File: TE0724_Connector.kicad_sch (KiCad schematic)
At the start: 1 part, among them J1 SS5-80-3.50-X-D-K-XX

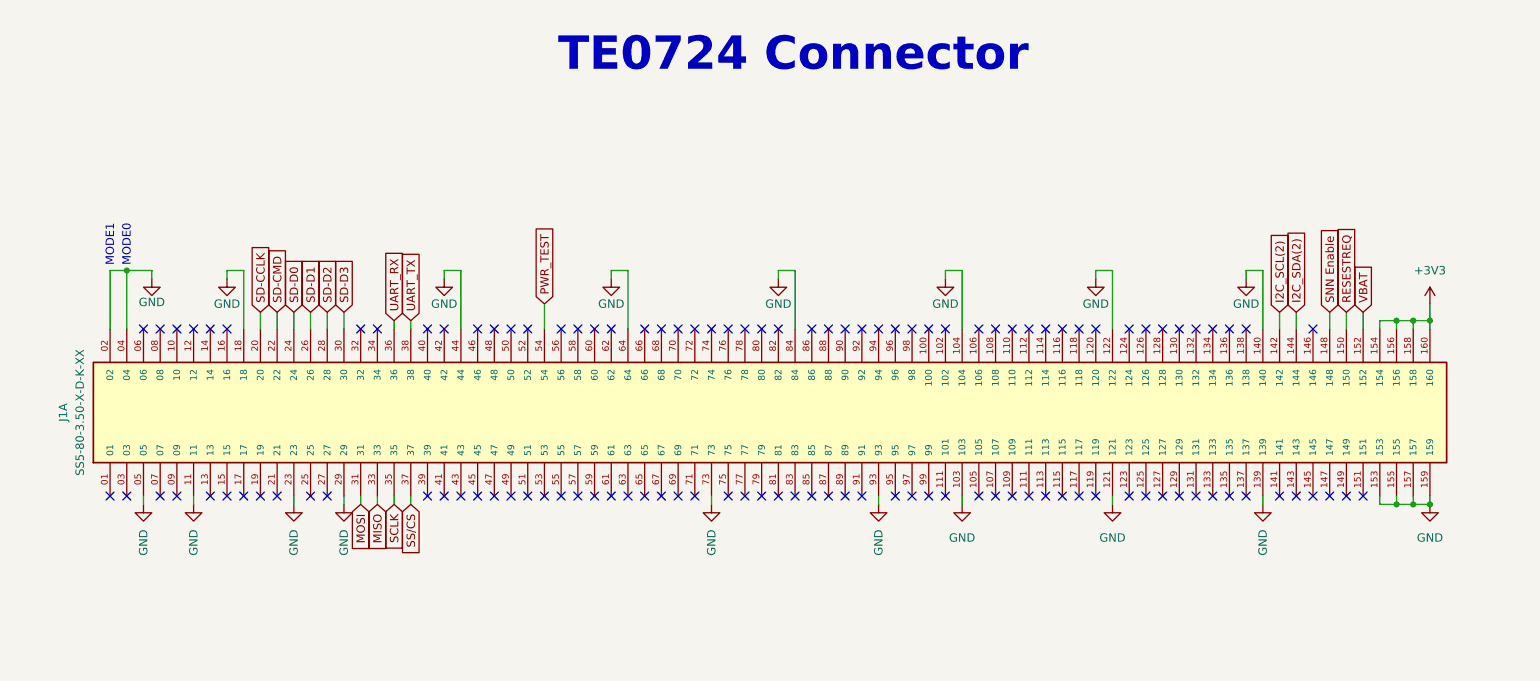
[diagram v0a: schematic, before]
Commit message: Fixed GND issues with connector and mounting holes
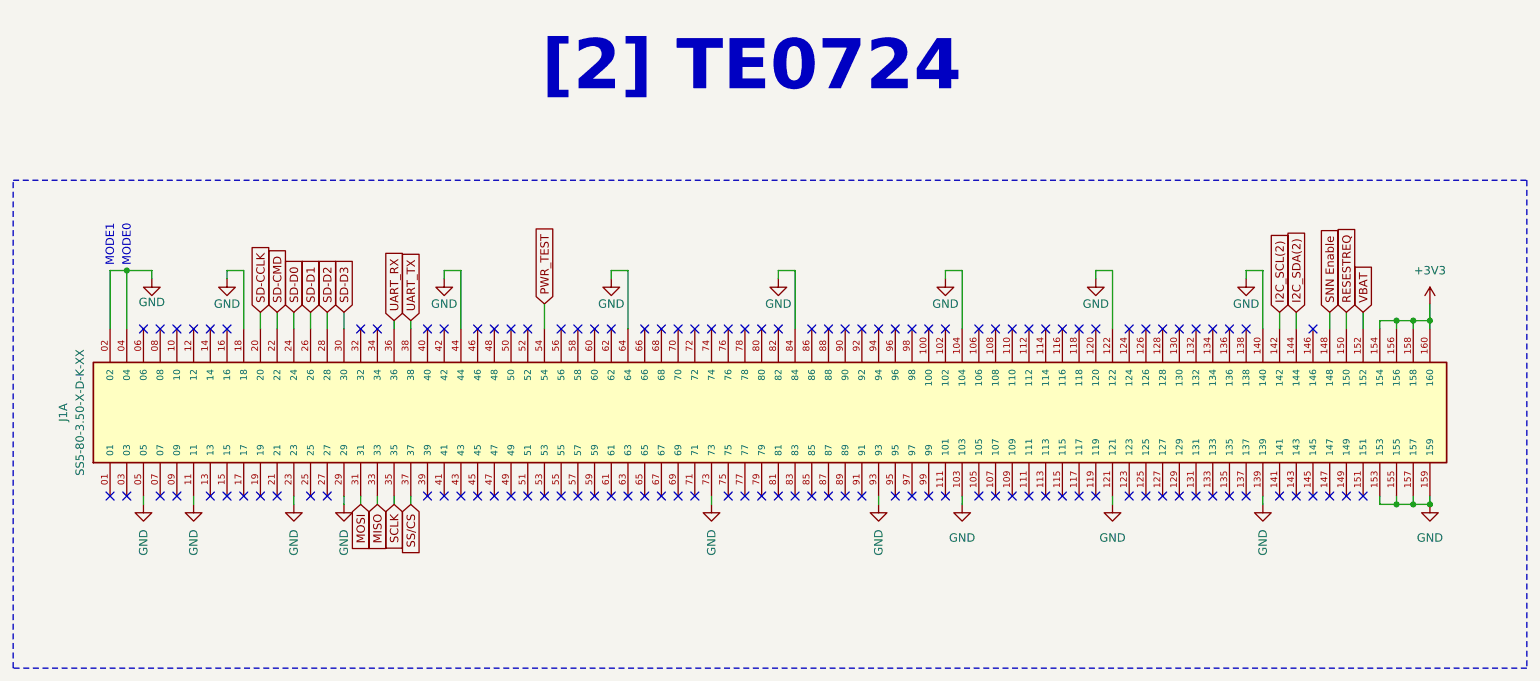
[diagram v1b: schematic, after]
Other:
- note added: "[2] TE0724"
- note removed: "TE0724 Connector"
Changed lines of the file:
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@@
 	(generator_version "9.0")
 	(paper "A4")
+	(rectangle
+		(start 34.798 44.704)
+		(end 264.922 118.872)
+		(stroke
+			(width 0)
+			(type dash)
+		)
+		(fill
+			(type none)
+		)
+	)
 	(text "MODE0"
 		(exclude_from_sim no)
@@
 		)
 	)
-	(text "TE0724 Connector"
+	(text "[2] TE0724"
 		(exclude_from_sim no)
-		(at 153.416 25.654 0)
+		(at 147.066 27.432 0)
 		(effects
 			(font
-				(size 5.08 5.08)
-				(thickness 0.508)
+				(size 7.62 7.62)
+				(thickness 1.524)
 				(bold yes)
 			)
